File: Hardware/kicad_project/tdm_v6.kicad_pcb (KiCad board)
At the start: 4 copper layers, 65 x 100 mm, 193 parts, among them J1 picoprobe_debug, J2 USB_C_Receptacle_USB2.0, J3 line_in, J4 headphone_out, J5 midi_in, J6 midi_out, J7 battery, J8 Conn_01x03_Male, Q1 DMG2305UX-13, Q2 Q_PMOS_GSD, Q3 Q_NPN_BEC, SW1 spst_4_pin_internal, SW10 spst_4_pin_internal, SW11 spst_4_pin_internal, SW12 spst_4_pin_internal, SW13 spst_4_pin_internal, SW14 spst_4_pin_internal, SW15 spst_4_pin_internal, SW16 spst_4_pin_internal, SW17 spst_4_pin_internal, SW18 spst_4_pin_internal, SW19 spst_4_pin_internal, SW2 spst_4_pin_internal, SW20 spst_4_pin_internal, SW21 spst_4_pin_internal, SW22 spst_4_pin_internal, SW23 spst_4_pin_internal, SW24 spst_4_pin_internal, SW25 spst_4_pin_internal, SW26 spst_4_pin_internal, SW27 spst_4_pin_internal, SW3 spst_4_pin_internal, SW4 spst_4_pin_internal, SW5 spst_4_pin_internal, SW6 spst_4_pin_internal, SW7 spst_4_pin_internal, SW8 spst_4_pin_internal, SW9 spst_4_pin_internal, U1 W25Q32JVSS, U2 RP2040, U3 TLV320AIC3204, U4 AP3722AT_mic, U5 6N137, U6 MCP73831T-2ATI_OT, U7 AMS1117-3.3, Y1 Crystal_GND24

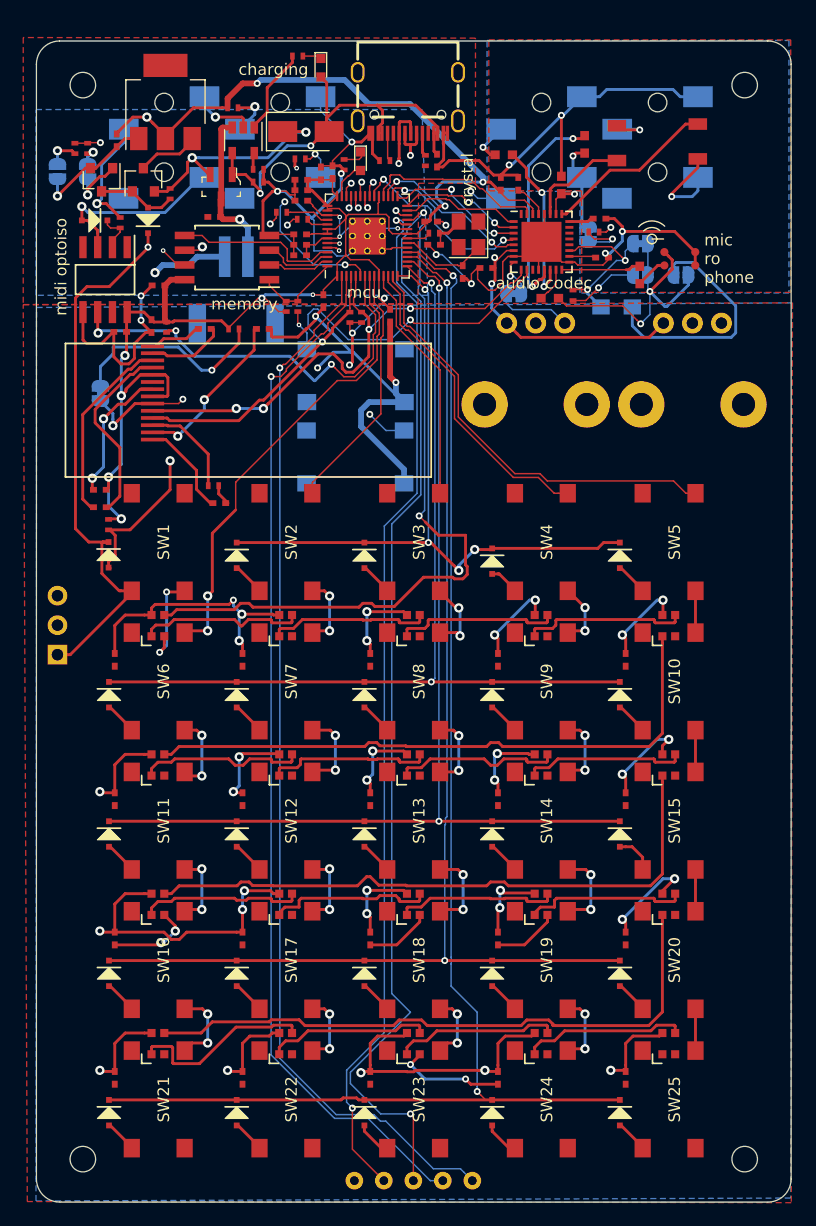
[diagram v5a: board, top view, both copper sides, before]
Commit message: new hardware rev
reworked power system
added amp
new LDOS (less dropout)
dedicated LDO for audio system
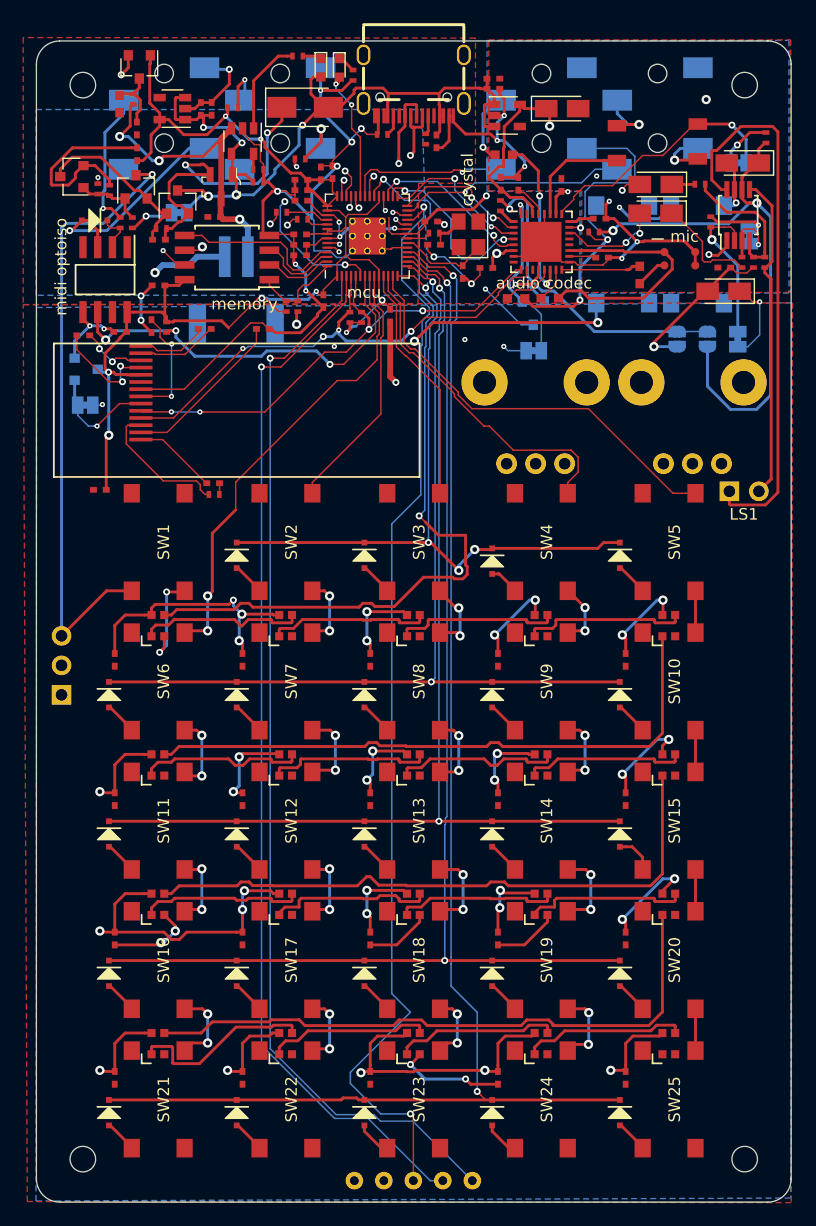
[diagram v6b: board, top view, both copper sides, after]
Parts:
- removed D51: LED, LEDs:LED_0603
- removed the R23 at (37.7, 41.1)
- added C4: 1u, Capacitors_Tantalum_SMD:CP_Tantalum_Case-A_EIA-3216-18_Reflow, F.Cu at (92.5, 53.4)
- added C4: 10u, RandomJunk:C_0402_NoSilk, F.Cu at (92.5, 51.4)
- added C5: 100n, RandomJunk:C_0402_NoSilk, F.Cu at (72.6, 36.0)
- added C59: 10n, RandomJunk:C_0402_NoSilk, F.Cu at (43.8, 49.0)
- added C60: 100n, RandomJunk:C_0402_NoSilk, F.Cu at (47.5, 37.7)
- added C61: 10u, RandomJunk:C_0402_NoSilk, F.Cu at (42.0, 41.6)
- added C62: 100n, RandomJunk:C_0402_NoSilk, F.Cu at (41.9, 39.4)
- added C63: 1u, RandomJunk:C_0402_NoSilk, F.Cu at (72.6, 35.1)
- added C64: 1u, RandomJunk:C_0402_NoSilk, F.Cu at (48.4, 37.7)
- added C65: 470nf, Capacitors_Tantalum_SMD:CP_Tantalum_Case-A_EIA-3216-18_Reflow, F.Cu at (86.6, 46.7)
- added C66: 1u, Capacitors_Tantalum_SMD:CP_Tantalum_Case-A_EIA-3216-18_Reflow, F.Cu at (94.1, 42.4)
- added C67: 470nf, Capacitors_Tantalum_SMD:CP_Tantalum_Case-A_EIA-3216-18_Reflow, F.Cu at (86.6, 44.2)
- added LS1: Speaker, Connector_PinHeader_2.54mm:PinHeader_1x02_P2.54mm_Horizontal, F.Cu at (93.0, 70.6)
- added Q4: Q_NMOS_GSD, TO_SOT_Packages_SMD:SOT-23, F.Cu at (42.1, 34.1)
- added R23: 20k, RandomJunk:R_0402_NoSilk, F.Cu at (91.4, 47.4)
- added R23: 10k, RandomJunk:R_0402_NoSilk, F.Cu at (95.0, 50.9)
- added R27: 1m, RandomJunk:R_0402_NoSilk, F.Cu at (39.6, 44.7)
- added R28: 1m, RandomJunk:R_0402_NoSilk, F.Cu at (41.6, 36.9)
- added R29: 750k, RandomJunk:C_0603_nosilk, F.Cu at (40.5, 37.3)
- added R30: 20k, RandomJunk:R_0402_NoSilk, F.Cu at (90.4, 44.2)
- added R31: 1k, RandomJunk:R_0402_NoSilk, F.Cu at (60.5, 34.8)
- added U10: apx804SR, TO_SOT_Packages_SMD:SOT-23, B.Cu at (37.6, 60.1)
- added U11: ME6211C, TO_SOT_Packages_SMD:SOT-23-5, F.Cu at (45.0, 37.7)
- added U8: LM4890, Housings_SSOP:MSOP-8_3x3mm_Pitch0.65mm, F.Cu at (93.7, 46.8)
- added U9: ME6211C, TO_SOT_Packages_SMD:SOT-23-5, F.Cu at (73.8, 38.3)
- C1, C2, C3: footprint Capacitors_SMD:C_0402_NoSilk -> RandomJunk:C_0402_NoSilk
- C40: footprint RandomJunk:C_0603_nosilk -> RandomJunk:C_0402_NoSilk
- C58: footprint RandomJunk:C_0402_NoSilk -> Capacitors_Tantalum_SMD:CP_Tantalum_Case-A_EIA-3216-18_Reflow
- D1: value D -> BAT54C; footprint RandomJunk:D_SOD-323F_less_silk -> TO_SOT_Packages_SMD:SOT-23
- D2: value D -> LED; footprint RandomJunk:D_SOD-323F_less_silk -> LEDs:LED_0603
- JP1, JP2: value SolderJumper_2_Bridged -> SolderJumper_2_Open; footprint Jumper:SolderJumper-2_P1.3mm_Bridged_RoundedPad1.0x1.5mm -> Jumper:SolderJumper-2_P1.3mm_Open_RoundedPad1.0x1.5mm
- JP3, JP5, JP8: value SolderJumper_2_Open -> SolderJumper_2_Bridged; footprint Jumper:SolderJumper-2_P1.3mm_Open_RoundedPad1.0x1.5mm -> Jumper:SolderJumper-2_P1.3mm_Bridged_Pad1.0x1.5mm
- JP4, JP6, JP7: footprint Jumper:SolderJumper-2_P1.3mm_Bridged_RoundedPad1.0x1.5mm -> Jumper:SolderJumper-2_P1.3mm_Bridged_Pad1.0x1.5mm
- Q3: value Q_NPN_BEC -> Q_NMOS_GSD
- R21, R22: value 100k -> 20k; footprint Resistors_SMD:R_0402_NoSilk -> RandomJunk:R_0402_NoSilk
- R24: footprint Resistors_SMD:R_0402_NoSilk -> RandomJunk:R_0402_NoSilk
- R25: value dnf -> 100k; footprint Resistors_SMD:R_0805_HandSoldering -> RandomJunk:R_0402_NoSilk; moved to F.Cu
- R26: value 10k -> 330; footprint Resistors_SMD:R_0402_NoSilk -> RandomJunk:R_0402_NoSilk
- R8: value 1k -> 100k
- R9: value 1k -> 10k
- U7: value AMS1117-3.3 -> apx804SR; footprint TO_SOT_Packages_SMD:SOT-223 -> TO_SOT_Packages_SMD:SOT-23; moved to B.Cu
- moved R22 60.9 mm to (96.0, 50.9)
- moved JP8 59.8 mm to (94.7, 48.6), turned to 90 degrees
- moved JP7 57.8 mm to (93.7, 57.5), turned to 90 degrees
- moved JP5 52.5 mm to (37.5, 63.2)
- moved R21 49.6 mm to (94.0, 50.9)
- moved R14 48.7 mm to (96.1, 40.2), turned to 90 degrees
- moved D2 46.4 mm to (59.4, 34.2)
- moved R25 39.8 mm to (44.0, 48.0), turned to 0 degrees
- moved C58 38.5 mm to (78.6, 37.7), turned to 0 degrees
- moved U7 36.5 mm to (76.1, 55.3), turned to 270 degrees
- moved SW27 34.2 mm to (90.2, 50.2), turned to 270 degrees
- moved SW26 25.2 mm to (83.8, 50.2), turned to 270 degrees
- moved R8 18.9 mm to (41.5, 47.5), turned to 90 degrees
- moved JP2 17.1 mm to (91.1, 57.5), turned to 90 degrees
- moved JP6 17.0 mm to (45.6, 46.6), turned to 180 degrees
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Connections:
- C40 pad 1: +3V3 -> +3V3A
- C41 pad 1: +3V3 -> +3V3A
- C42 pad 1: +3V3 -> +3V3A
- C54 pad 1: +3V3 -> Net-(C54-Pad1)
- C58 pad 1: +3V3 -> +3V3A
- D1 pad 2: Net-(D1-Pad2) -> Net-(C59-Pad2)
- D2 pad 1: Net-(D1-Pad1) -> Net-(D2-Pad1)
- D2 pad 2: power_gpio -> Net-(D2-Pad2)
- D53 pad 1: Net-(D53-Pad1) -> Net-(C59-Pad1)
- J4 pad 4: Net-(J4-Pad4) -> headphone_detect
- J8 pad 1: Net-(D1-Pad1) -> Net-(J8-Pad1)
- J8 pad 3: Net-(J8-Pad3) -> Net-(D1-Pad3)
- JP1 pad 1: Net-(JP1-Pad1) -> GND
- JP1 pad 2: Net-(C39-Pad2) -> Net-(JP1-Pad2)
- JP2 pad 1: GND -> +3V3A
- JP2 pad 2: Net-(JP2-Pad2) -> Net-(JP1-Pad2)
- JP3 pad 2: Net-(C45-Pad2) -> subsystem_reset
- JP4 pad 2: Net-(C45-Pad2) -> Net-(C49-Pad2)
- JP5 pad 2: Net-(C45-Pad2) -> subsystem_reset
- JP6 pad 1: Net-(JP6-Pad1) -> VBUS
- JP6 pad 2: screen_reset -> Net-(JP6-Pad2)
- JP8 pad 2: GND -> Net-(JP8-Pad2)
- LCD1 pad 8: +3V3 -> Net-(C54-Pad1)
- LCD1 pad 9: screen_reset -> Net-(JP5-Pad1)
- Q1 pad 2: Net-(D53-Pad1) -> Net-(C59-Pad1)
- Q2 pad 1: Net-(D1-Pad2) -> Net-(C59-Pad2)
- Q2 pad 2: Net-(D53-Pad1) -> Net-(C59-Pad1)
- Q2 pad 3: Net-(Q2-Pad3) -> VBUS
- Q3 pad 1: Net-(JP7-Pad2) -> Net-(D1-Pad1)
- Q3 pad 3: Net-(D1-Pad2) -> Net-(C59-Pad2)
- R14 pad 1: Net-(JP6-Pad1) -> +3V3A
- R14 pad 2: +3V3 -> Net-(JP4-Pad1)
- R21 pad 1: Net-(D1-Pad2) -> Net-(C65-Pad1)
- R21 pad 2: Net-(D53-Pad1) -> Net-(JP8-Pad1)
- R22 pad 1: power_gpio -> Net-(LS1-Pad2)
- R22 pad 2: +3V3 -> Net-(R22-Pad2)
- R24 pad 1: Net-(JP1-Pad1) -> Net-(C39-Pad2)
- R24 pad 2: +3V3 -> +3V3A
- R25 pad 1: Net-(JP5-Pad1) -> Net-(C59-Pad2)
- R25 pad 2: Net-(JP4-Pad1) -> Net-(C59-Pad1)
- R26 pad 2: Net-(JP8-Pad1) -> Net-(D1-Pad1)
- R8 pad 1: Net-(D51-Pad1) -> Net-(JP6-Pad2)
- R8 pad 2: GND -> Net-(D1-Pad1)
- R9 pad 1: Net-(JP3-Pad1) -> Net-(R9-Pad1)
- R9 pad 2: Net-(JP4-Pad1) -> Net-(JP1-Pad2)
- SW1 pad 1: Net-(D1-Pad1) -> Net-(D1-Pad3)
- U2 pad 27: mclk -> headphone_detect
- U2 pad 32: codec_reset -> subsystem_reset
- U2 pad 36: power_gpio -> line_in_detect
- U2 pad 37: line_in_detect -> Net-(D2-Pad2)
- U2 pad 38: pot1 -> pot2
- U2 pad 39: pot2 -> pot1
- U2 pad 40: screen_reset -> bat_sense
- U2 pad 41: Net-(D51-Pad2) -> amp_control
- U3 pad 1: mclk -> Net-(R9-Pad1)
- U3 pad 19: Net-(JP4-Pad1) -> Net-(C45-Pad2)
- U3 pad 22: Net-(U3-Pad22) -> /AudioMidi/lineout_left
- U3 pad 23: Net-(U3-Pad23) -> /AudioMidi/lineout_right
- U3 pad 26: +3V3 -> +3V3A
- U3 pad 30: +3V3 -> +3V3A
- U3 pad 31: codec_reset -> Net-(U3-Pad31)
- U3 pad 32: Net-(U3-Pad32) -> Net-(JP3-Pad1)
- U3 pad 6: +3V3 -> +3V3A
- U3 pad 8: Net-(JP2-Pad2) -> Net-(U3-Pad8)
- U7 pad 1: GND -> Net-(JP3-Pad1)
- U7 pad 2: +3V3 -> GND
- U7 pad 3: Net-(Q2-Pad3) -> +3V3
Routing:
- net +3V3A: track 0.00 -> 92.2 mm, vias 0 -> 5
- net +3V3: track 384.9 -> 318.4 mm, vias 49 -> 43
- net subsystem_reset: track 0.00 -> 54.0 mm, vias 0 -> 3
- net Net-(D1-Pad3): track 0.00 -> 53.9 mm, vias 0 -> 1
- net Net-(LS1-Pad1): track 0.00 -> 47.7 mm
- net power_gpio: track 44.9 -> 0.00 mm, vias 2 -> 0
- net Net-(D1-Pad1): track 47.8 -> 5.87 mm, vias 1 -> 0
- net amp_control: track 0.00 -> 39.1 mm, vias 0 -> 2
- net screen_reset: track 35.7 -> 0.00 mm, vias 3 -> 0
- net VBUS: track 37.0 -> 69.6 mm, vias 2 -> 5
- net Net-(C59-Pad1): track 0.00 -> 28.1 mm, vias 0 -> 2
- net Net-(LS1-Pad2): track 0.00 -> 28.0 mm
- net bat_sense: track 0.00 -> 27.4 mm, vias 0 -> 2
- net Net-(JP1-Pad2): track 0.00 -> 27.3 mm, vias 0 -> 1
- net Net-(R6-Pad2): track 3.57 -> 30.4 mm, vias 1 -> 3
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- added copper zone on In2.Cu, net +3V3
- added copper zone on In2.Cu, net +3V3A
- removed copper zone on In2.Cu, net GND
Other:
- rule via_min_size: 0.4 -> 0.45
- board text added: "JLCJLCJLCJLC"
- board text added: "UBOOT"
- board text added: "V8"
- board text added: "a in"
- board text added: "a out"
- board text added: "mic"
- board text removed: "SAFEBOOT"
- board text removed: "audio in"
- board text removed: "audio out"
- board text removed: "charging"
- board text removed: "mic ro phone"

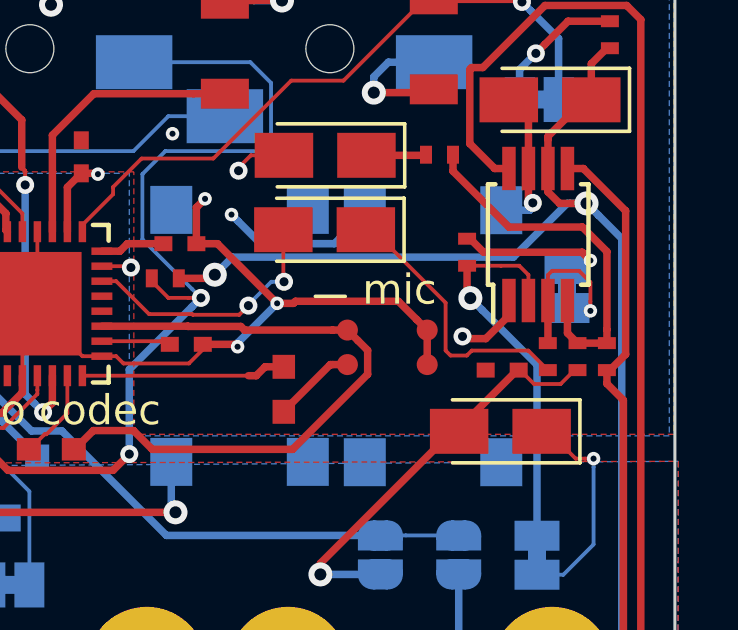
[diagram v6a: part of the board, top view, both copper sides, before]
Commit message: corrected pcb / fixed c4 position
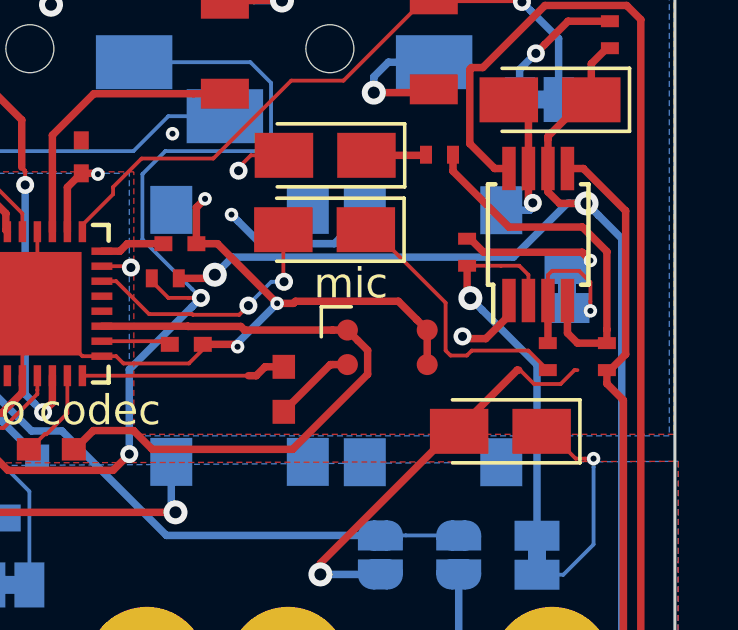
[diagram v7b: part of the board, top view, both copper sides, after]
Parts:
- removed the C4 at (92.5, 51.4)
- removed the R23 at (95.0, 50.9)
- C40: value .1uF -> 100n

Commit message: uhhh, just too many changes - most recently added the sample loop cutting
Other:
- net class Default removed
- board text added: "V9"
- board text removed: "V8"
